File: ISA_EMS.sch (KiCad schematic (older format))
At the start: 57 parts, among them J1 ISA BUS, J2 EMS Address, J3 ROM Config, U1 74HCT688, U10 74HCT32, U11 74HCT04, U12 74ACT245, U13 AS6C4008-55PCN, U14 AS6C4008-55PCN, U15 AS6C4008-55PCN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

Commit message: Begin removing useless components
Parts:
- removed C10, C16, C19, C20, C21, C38: 100nF, Capacitor_THT:C_Disc_D6.0mm_W2.5mm_P5.00mm, symbol Device:C_Small
- removed J3: ROM Config, Connector_PinHeader_2.54mm:PinHeader_2x07_P2.54mm_Vertical, symbol Connector_Generic:Conn_02x07_Odd_Even
- removed R1, R2: 10k, Resistor_THT:R_Axial_DIN0207_L6.3mm_D2.5mm_P10.16mm_Horizontal, symbol Device:R_Small
- removed RN1: 10k, Resistor_THT:R_Array_SIP6, symbol Device:R_Network05
- removed U1: 74HCT688, Package_DIP:DIP-20_W7.62mm_LongPads, symbol 74xx:74HCT688
- removed U13, U14, U15, U16: AS6C4008-55PCN, Package_DIP:DIP-32_W15.24mm, symbol Memory_RAM:AS6C4008-55PCN
- removed U2: SST39SF040, Package_DIP:DIP-32_W15.24mm_LongPads, symbol Memory_Flash:SST39SF040
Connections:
- net labels removed: COMPARATOR_A15, FLASH_A15, SW_A15, SW_A16, SW_A17, SW_A18, SW_ROM_EN, ~ROM-CS
- wire segments 801 -> 541
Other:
- note removed: "32K"
- note removed: "32K ROM bank"
- note removed: "64K"
- note removed: "64K ROM bank"
- note removed: "A000h"
- note removed: "A15"
- note removed: "A16"
- note removed: "A17"
- note removed: "A18"
- note removed: "A800h"
- note removed: "B000h"
- note removed: "B800h"
- note removed: "C000h"
- note removed: "C800h"
- note removed: "D000h"
- note removed: "D800h"
- note removed: "E000h"
- note removed: "E800h"
- note removed: "ENA"
- note removed: "F000h"
- note removed: "F800h"
- note removed: "If 32K mode is set, the A15 line will\nnot be used to address the content\nof the ROM (FLASH_A15 will be always\nlow), but will be decoded by the\n'688 to decide whether the ROM gets\nenabled or not.\n\nIn 64K mode, the A15 line will be used\nto address the content of the ROM,\nthe A15 jumper MUST be set, otherwise\nthe decoder will fail to enable the ROM\n(note how the COMPARATOR_A15 line\nwill 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"
- note removed: "Jumper ONE of these two to\nselect 32K or 64K ROM slot size"
- note removed: "Jumper to ENABLE the ROM"
- note removed: "Logic taken from https://www.lo-tech.co.uk/wiki/Lo-tech_ISA_ROM_Board"
- note removed: "ROM"
- note removed: "Remember that the comparator is\nhardwired to check for A19 to be HIGH!"
- note removed: "X"

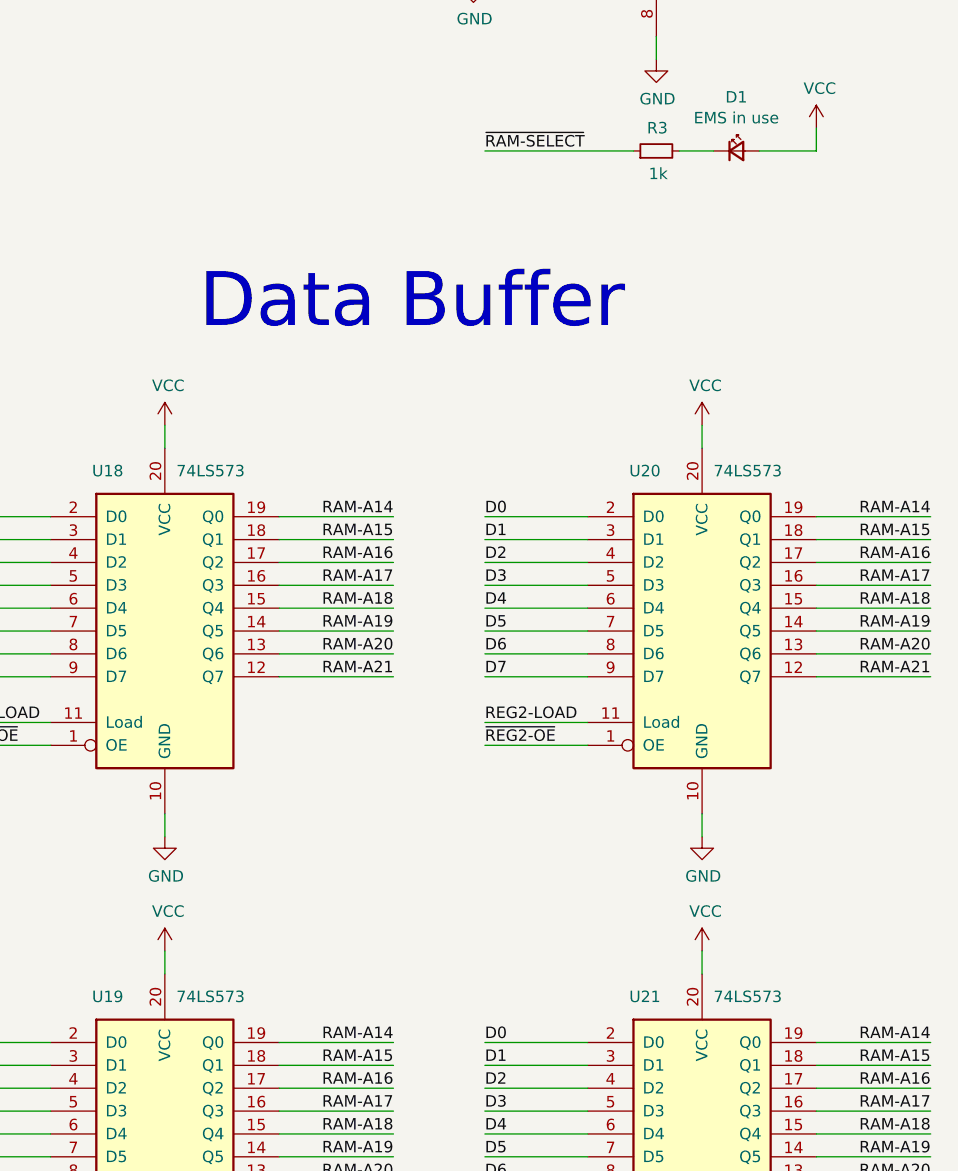
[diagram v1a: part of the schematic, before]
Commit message: Add silkscreen
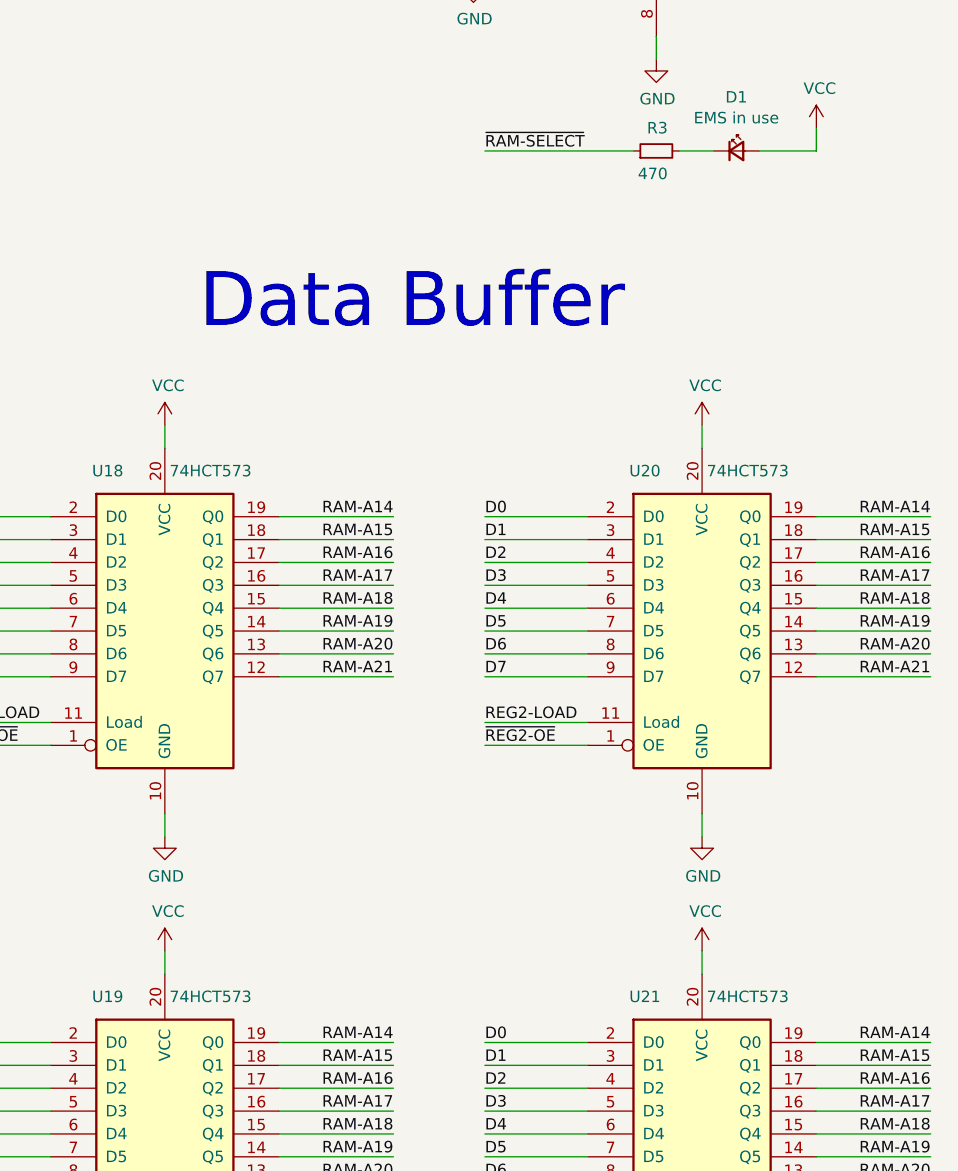
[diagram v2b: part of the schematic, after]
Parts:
- R3: value 1k -> 470
- U18, U19, U20, U21: value 74LS573 -> 74HCT573
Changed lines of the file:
@@
 P 13700 10200
 F 0 "U18" H 13450 10900 50  0000 C CNN
-F 1 "74LS573" H 13900 10900 50  0000 C CNN
+F 1 "74HCT573" H 13900 10900 50  0000 C CNN
 F 2 "Package_DIP:DIP-20_W7.62mm_LongPads" H 13700 10200 50  0001 C CNN
 F 3 "74xx/74hc573.pdf" H 13700 10200 50  0001 C CNN
@@
 P 13700 12500
 F 0 "U19" H 13450 13200 50  0000 C CNN
-F 1 "74LS573" H 13900 13200 50  0000 C CNN
+F 1 "74HCT573" H 13900 13200 50  0000 C CNN
 F 2 "Package_DIP:DIP-20_W7.62mm_LongPads" H 13700 12500 50  0001 C CNN
 F 3 "74xx/74hc573.pdf" H 13700 12500 50  0001 C CNN
@@
 P 16050 10200
 F 0 "U20" H 15800 10900 50  0000 C CNN
-F 1 "74LS573" H 16250 10900 50  0000 C CNN
+F 1 "74HCT573" H 16250 10900 50  0000 C CNN
 F 2 "Package_DIP:DIP-20_W7.62mm_LongPads" H 16050 10200 50  0001 C CNN
 F 3 "74xx/74hc573.pdf" H 16050 10200 50  0001 C CNN
@@
 P 16050 12500
 F 0 "U21" H 15800 13200 50  0000 C CNN
-F 1 "74LS573" H 16250 13200 50  0000 C CNN
+F 1 "74HCT573" H 16250 13200 50  0000 C CNN
 F 2 "Package_DIP:DIP-20_W7.62mm_LongPads" H 16050 12500 50  0001 C CNN
 F 3 "74xx/74hc573.pdf" H 16050 12500 50  0001 C CNN
@@
 P 15850 8100
 F 0 "R3" V 15950 8050 50  0000 L CNN
-F 1 "1k" V 15750 8050 50  0000 L CNN
+F 1 "470" V 15750 8050 50  0000 L CNN
 F 2 "Resistor_THT:R_Axial_DIN0207_L6.3mm_D2.5mm_P10.16mm_Horizontal" H 15850 8100 50  0001 C CNN
 F 3 "~" H 15850 8100 50  0001 C CNN
